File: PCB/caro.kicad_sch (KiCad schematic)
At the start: 9 parts, among them SW1 Power Switch, SW2 Control Button, U1 DFR0299

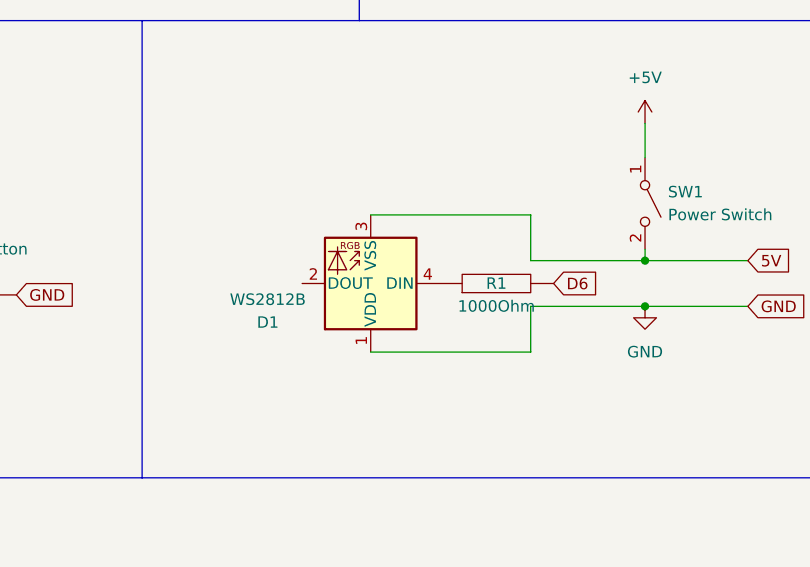
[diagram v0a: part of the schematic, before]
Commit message: Corrected inverted LED pins
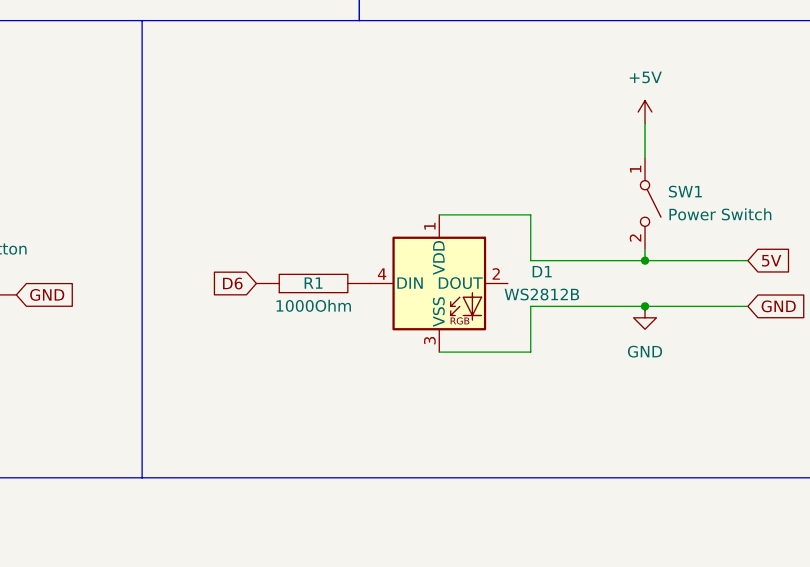
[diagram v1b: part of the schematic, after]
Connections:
- net 5V: now also D1.1 (VDD); no longer D1.3 (VSS)
- net D6: now also R1.1; no longer R1.2
- net GND: now also D1.3 (VSS); no longer D1.1 (VDD)
- net at D1.4 (DIN): now also R1.2; no longer R1.1
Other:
- moved on the sheet: D1, R1
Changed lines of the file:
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@@
     (stroke (width 0) (type default) (color 0 0 0 0))
   )
-  (wire (pts (xy 240.03 99.06) (xy 222.25 99.06))
-    (stroke (width 0) (type default) (color 0 0 0 0))
-  )
-  (wire (pts (xy 240.03 114.3) (xy 222.25 114.3))
+  (wire (pts (xy 240.03 99.06) (xy 229.87 99.06))
+    (stroke (width 0) (type default) (color 0 0 0 0))
+  )
+  (wire (pts (xy 240.03 114.3) (xy 229.87 114.3))
     (stroke (width 0) (type default) (color 0 0 0 0))
   )
@@
     )
   )
-  (global_label "D6" (shape input) (at 242.57 106.68 0) (fields_autoplaced)
-    (effects (font (size 1.27 1.27)) (justify left))
-    (property "Intersheet References" "${INTERSHEET_REFS}" (id 0) (at 247.4626 106.6006 0)
-      (effects (font (size 1.27 1.27)) (justify left) hide)
+  (global_label "D6" (shape input) (at 209.55 106.68 180) (fields_autoplaced)
+    (effects (font (size 1.27 1.27)) (justify right))
+    (property "Intersheet References" "${INTERSHEET_REFS}" (id 0) (at 204.6574 106.7594 0)
+      (effects (font (size 1.27 1.27)) (justify right) hide)
     )
   )
@@
     (pin "1")
   )
-  (symbol (lib_id "pspice:R") (at 236.22 106.68 90) (unit 1)
-    (in_bom yes) (on_board yes)
-    (property "Reference" "R1" (id 0) (at 236.22 106.68 90))
-    (property "Value" "1000Ohm" (id 1) (at 236.22 109.22 90))
-    (property "Footprint" "Resistor_THT:R_Axial_DIN0309_L9.0mm_D3.2mm_P20.32mm_Horizontal" (id 2) (at 236.22 106.68 0)
-      (effects (font (size 1.27 1.27)) hide)
-    )
-    (property "Datasheet" "~" (id 3) (at 236.22 106.68 0)
+  (symbol (lib_id "pspice:R") (at 215.9 106.68 90) (unit 1)
+    (in_bom yes) (on_board yes)
+    (property "Reference" "R1" (id 0) (at 215.9 106.68 90))
+    (property "Value" "1000Ohm" (id 1) (at 215.9 109.22 90))
+    (property "Footprint" "Resistor_THT:R_Axial_DIN0309_L9.0mm_D3.2mm_P20.32mm_Horizontal" (id 2) (at 215.9 106.68 0)
+      (effects (font (size 1.27 1.27)) hide)
+    )
+    (property "Datasheet" "~" (id 3) (at 215.9 106.68 0)
       (effects (font (size 1.27 1.27)) hide)
     )
@@
     (pin "9")
   )
-  (symbol (lib_id "LED:WS2812B") (at 222.25 106.68 180) (unit 1)
-    (in_bom yes) (on_board yes) (fields_autoplaced)
-    (property "Reference" "D1" (id 0) (at 210.82 111.0107 0))
-    (property "Value" "WS2812B" (id 1) (at 210.82 108.4707 0))
-    (property "Footprint" "Connector_PinHeader_2.54mm:PinHeader_1x03_P2.54mm_Vertical" (id 2) (at 220.98 99.06 0)
+  (symbol (lib_id "LED:WS2812B") (at 229.87 106.68 0) (unit 1)
+    (in_bom yes) (on_board yes)
+    (property "Reference" "D1" (id 0) (at 241.3 105.41 0))
+    (property "Value" "WS2812B" (id 1) (at 241.3 107.95 0))
+    (property "Footprint" "Connector_PinHeader_2.54mm:PinHeader_1x03_P2.54mm_Vertical" (id 2) (at 231.14 114.3 0)
       (effects (font (size 1.27 1.27)) (justify left top) hide)
     )
-    (property "Datasheet" "https://cdn-shop.adafruit.com/datasheets/WS2812B.pdf" (id 3) (at 219.71 97.155 0)
+    (property "Datasheet" "https://cdn-shop.adafruit.com/datasheets/WS2812B.pdf" (id 3) (at 232.41 116.205 0)
       (effects (font (size 1.27 1.27)) (justify left top) hide)
     )

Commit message: Bump to v1.1
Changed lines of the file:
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@@
+    (stroke (width 0) (type default) (color 0 0 0 0))
+  )
+  (wire (pts (xy 207.01 106.68) (xy 209.55 106.68))
     (stroke (width 0) (type default) (color 0 0 0 0))
   )
@@
     )
   )
-  (global_label "D6" (shape input) (at 209.55 106.68 180) (fields_autoplaced)
+  (global_label "D6" (shape input) (at 207.01 106.68 180) (fields_autoplaced)
     (effects (font (size 1.27 1.27)) (justify right))
-    (property "Intersheet References" "${INTERSHEET_REFS}" (id 0) (at 204.6574 106.7594 0)
+    (property "Intersheet References" "${INTERSHEET_REFS}" (id 0) (at 202.1174 106.7594 0)
       (effects (font (size 1.27 1.27)) (justify right) hide)
     )

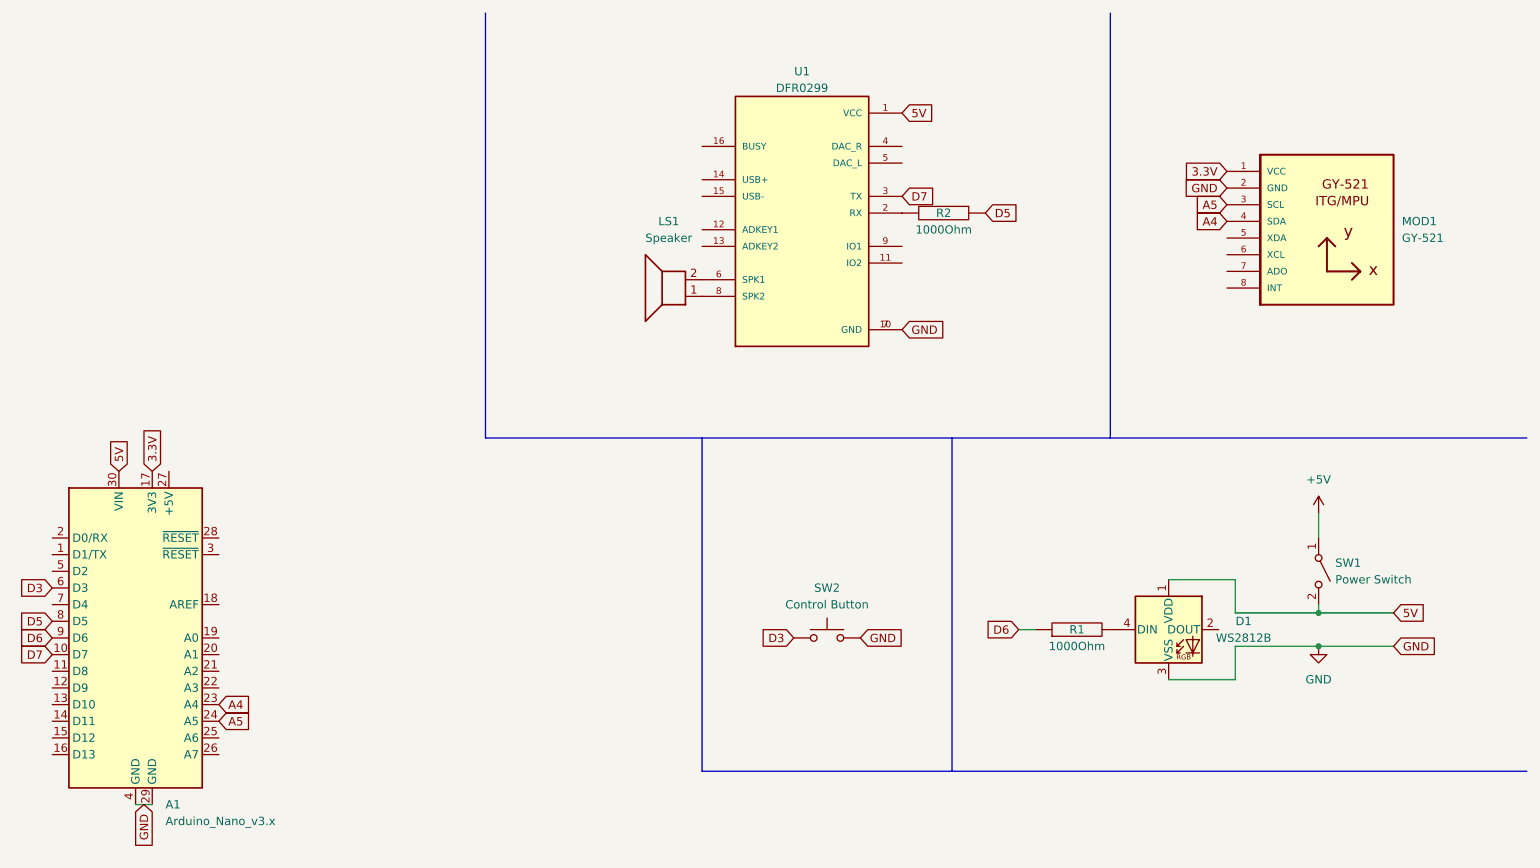
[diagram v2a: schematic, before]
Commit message: Updated annotations Added missing control LED Reduced resistor sizes
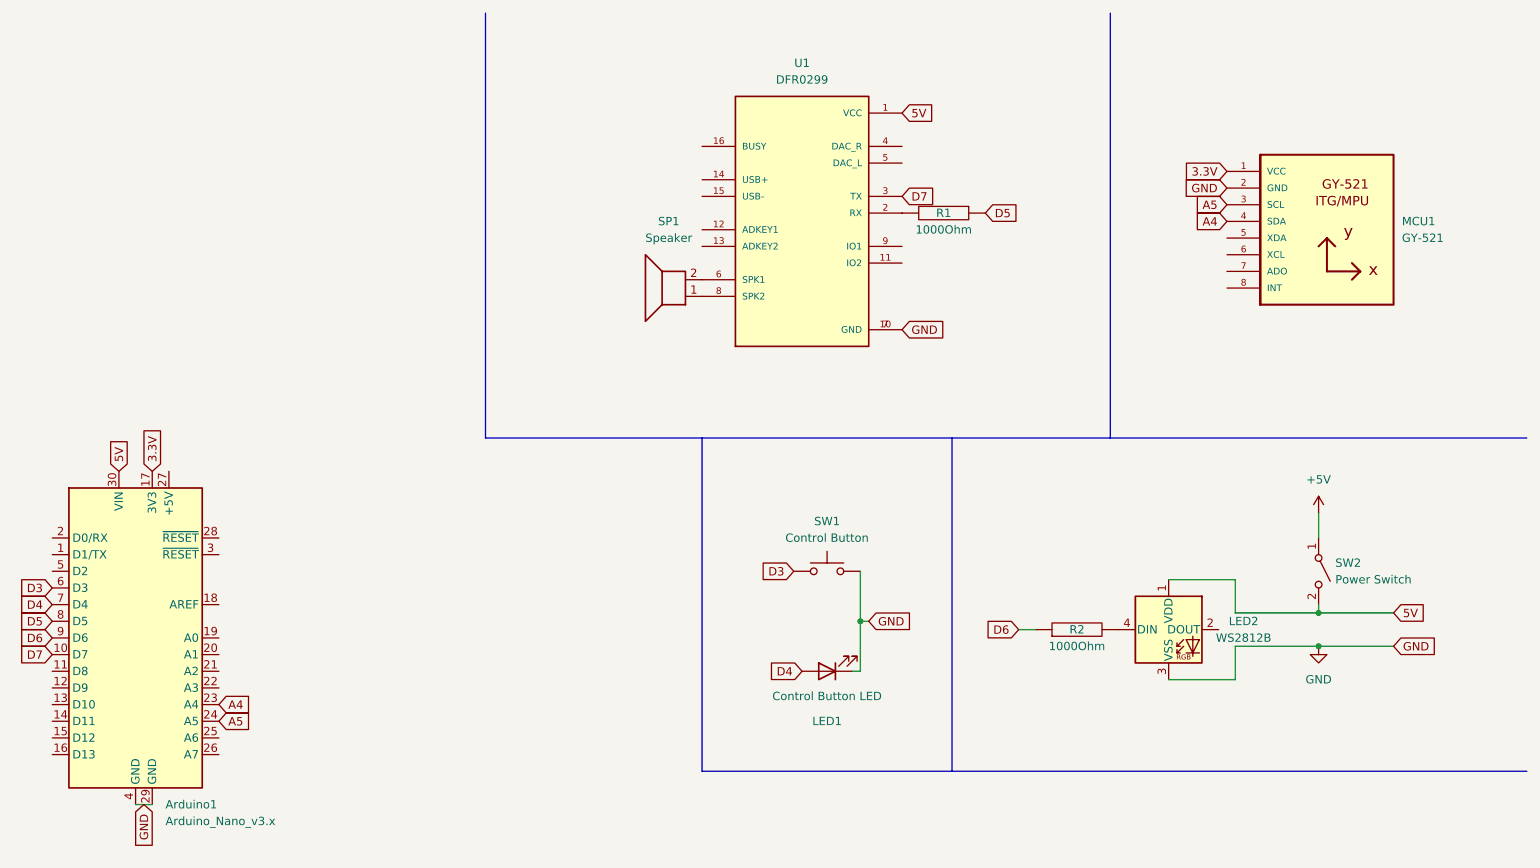
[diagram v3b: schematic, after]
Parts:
- added LED1: Control Button LED, Connector_PinHeader_2.54mm:PinHeader_2x01_P2.54mm_Vertical, symbol Device:LED
- R1: renamed from R2; footprint Resistor_THT:R_Axial_DIN0309_L9.0mm_D3.2mm_P20.32mm_Horizontal -> Resistor_THT:R_Axial_DIN0207_L6.3mm_D2.5mm_P10.16mm_Horizontal
- R2: renamed from R1; footprint Resistor_THT:R_Axial_DIN0309_L9.0mm_D3.2mm_P20.32mm_Horizontal -> Resistor_THT:R_Axial_DIN0207_L6.3mm_D2.5mm_P10.16mm_Horizontal
- renumbered A1 to Arduino1, D1 to LED2, MOD1 to MCU1, LS1 to SP1, SW2 to SW1, SW1 to SW2
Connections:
- net GND: now also LED1.1 (K)
- net D4: now reaches Arduino1.7 (D4)
- net D4: now also LED1.2 (A)
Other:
- moved on the sheet: SW1

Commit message: Revision v1.4 Swapped MCU and SDCard
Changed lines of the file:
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@@
     )
     (pin "1")
-    (pin "2")
     (pin "3")
     (pin "4")

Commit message: Corrected worng annotation
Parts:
- renumbered Arduino1 to U2
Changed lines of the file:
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@@
   (symbol (lib_id "MCU_Module:Arduino_Nano_v3.x") (at 72.39 107.95 0) (unit 1)
     (in_bom yes) (on_board yes) (fields_autoplaced)
-    (property "Reference" "Arduino1" (id 0) (at 76.9494 133.35 0)
+    (property "Reference" "U2" (id 0) (at 76.9494 133.35 0)
       (effects (font (size 1.27 1.27)) (justify left))
     )
@@
       (reference "#PWR02") (unit 1) (value "GND") (footprint "")
     )
-    (path "/ced11390-2682-4807-887b-321629abfbac"
-      (reference "Arduino1") (unit 1) (value "Arduino_Nano_v3.x") (footprint "Module:Arduino_Nano")
-    )
     (path "/ae1091f9-be9a-4c5e-a932-4d89f59d1190"
       (reference "LED1") (unit 1) (value "Control Button LED") (footprint "Connector_PinHeader_2.54mm:PinHeader_2x01_P2.54mm_Vertical")
@@
       (reference "U1") (unit 1) (value "DFR0299") (footprint "DFR0299:MODULE_DFR0299")
     )
+    (path "/ced11390-2682-4807-887b-321629abfbac"
+      (reference "U2") (unit 1) (value "Arduino_Nano_v3.x") (footprint "Module:Arduino_Nano")
+    )
   )

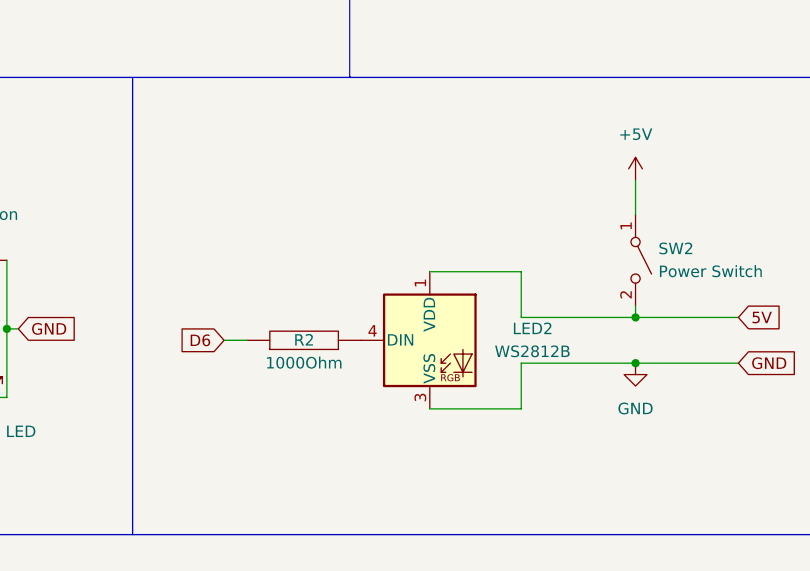
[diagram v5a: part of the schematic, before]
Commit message: Revision udate to v1.5 Swapped WS2812b to WS2811
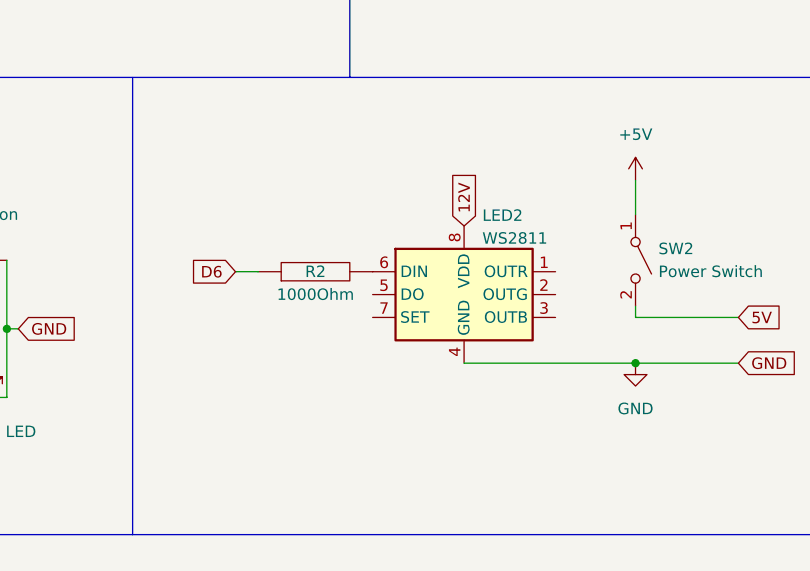
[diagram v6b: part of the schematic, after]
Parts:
- removed LED2: WS2812B, Connector_PinHeader_2.54mm:PinHeader_1x03_P2.54mm_Vertical, symbol LED:WS2812B
- added LED2: WS2811, Connector_PinHeader_2.54mm:PinHeader_1x02_P2.54mm_Vertical, symbol Driver_LED:WS2811
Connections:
- net GND: now also LED2.4 (GND)
- net at R2.2: now also LED2.6 (DIN)
- new net 12V: LED2.8 (VDD)
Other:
- moved on the sheet: R2
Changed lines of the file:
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@@
     (title "Carolyns Lightsaber")
   )
-  (junction (at 252.73 104.14) (diameter 0) (color 0 0 0 0)
-  )
   (junction (at 182.88 105.41) (diameter 0) (color 0 0 0 0)
   )
@@
     (stroke (width 0) (type default) (color 0 0 0 0))
   )
-  (wire (pts (xy 240.03 104.14) (xy 240.03 99.06))
-    (stroke (width 0) (type default) (color 0 0 0 0))
-  )
   (wire (pts (xy 182.88 97.79) (xy 182.88 105.41))
     (stroke (width 0) (type default) (color 0 0 0 0))
@@
     (stroke (width 0) (type default) (color 0 0 0 0))
   )
-  (wire (pts (xy 240.03 99.06) (xy 229.87 99.06))
-    (stroke (width 0) (type default) (color 0 0 0 0))
-  )
-  (wire (pts (xy 240.03 114.3) (xy 229.87 114.3))
-    (stroke (width 0) (type default) (color 0 0 0 0))
-  )
-  (wire (pts (xy 240.03 109.22) (xy 240.03 114.3))
-    (stroke (width 0) (type default) (color 0 0 0 0))
-  )
   (polyline (pts (xy 125.73 77.47) (xy 220.98 77.47))
     (stroke (width 0) (type default) (color 0 0 0 0))
@@
     (stroke (width 0) (type default) (color 0 0 0 0))
   )
-  (wire (pts (xy 207.01 106.68) (xy 209.55 106.68))
+  (wire (pts (xy 208.28 99.06) (xy 210.82 99.06))
     (stroke (width 0) (type default) (color 0 0 0 0))
   )
@@
     (stroke (width 0) (type default) (color 0 0 0 0))
   )
-  (wire (pts (xy 252.73 109.22) (xy 240.03 109.22))
-    (stroke (width 0) (type default) (color 0 0 0 0))
-  )
-  (wire (pts (xy 240.03 104.14) (xy 252.73 104.14))
+  (wire (pts (xy 233.68 109.22) (xy 252.73 109.22))
     (stroke (width 0) (type default) (color 0 0 0 0))
   )
@@
     )
   )
-  (global_label "D6" (shape input) (at 207.01 106.68 180) (fields_autoplaced)
-    (effects (font (size 1.27 1.27)) (justify right))
-    (property "Intersheet References" "${INTERSHEET_REFS}" (id 0) (at 202.1174 106.7594 0)
+  (global_label "D6" (shape input) (at 208.28 99.06 180) (fields_autoplaced)
+    (effects (font (size 1.27 1.27)) (justify right))
+    (property "Intersheet References" "${INTERSHEET_REFS}" (id 0) (at 203.3874 99.1394 0)
       (effects (font (size 1.27 1.27)) (justify right) hide)
     )
@@
     (effects (font (size 1.27 1.27)) (justify left))
     (property "Intersheet References" "${INTERSHEET_REFS}" (id 0) (at 270.4436 109.1406 0)
+      (effects (font (size 1.27 1.27)) (justify left) hide)
+    )
+  )
+  (global_label "12V" (shape input) (at 233.68 93.98 90) (fields_autoplaced)
+    (effects (font (size 1.27 1.27)) (justify left))
+    (property "Intersheet References" "${INTERSHEET_REFS}" (id 0) (at 233.6006 88.0593 90)
       (effects (font (size 1.27 1.27)) (justify left) hide)
     )
@@
     (pin "1")
   )
-  (symbol (lib_id "pspice:R") (at 215.9 106.68 90) (unit 1)
+  (symbol (lib_id "pspice:R") (at 217.17 99.06 90) (unit 1)
     (in_bom yes) (on_board yes)
-    (property "Reference" "R2" (id 0) (at 215.9 106.68 90))
-    (property "Value" "1000Ohm" (id 1) (at 215.9 109.22 90))
-    (property "Footprint" "Resistor_THT:R_Axial_DIN0207_L6.3mm_D2.5mm_P10.16mm_Horizontal" (id 2) (at 215.9 106.68 0)
-      (effects (font (size 1.27 1.27)) hide)
-    )
-    (property "Datasheet" "~" (id 3) (at 215.9 106.68 0)
+    (property "Reference" "R2" (id 0) (at 217.17 99.06 90))
+    (property "Value" "1000Ohm" (id 1) (at 217.17 101.6 90))
+    (property "Footprint" "Resistor_THT:R_Axial_DIN0207_L6.3mm_D2.5mm_P10.16mm_Horizontal" (id 2) (at 217.17 99.06 0)
+      (effects (font (size 1.27 1.27)) hide)
+    )
+    (property "Datasheet" "~" (id 3) (at 217.17 99.06 0)
       (effects (font (size 1.27 1.27)) hide)
     )
@@
     (pin "1")
     (pin "2")
+  )
+  (symbol (lib_id "Driver_LED:WS2811") (at 233.68 101.6 0) (unit 1)
+    (in_bom yes) (on_board yes) (fields_autoplaced)
+    (property "Reference" "LED2" (id 0) (at 235.6994 92.8202 0)
+      (effects (font (size 1.27 1.27)) (justify left))
+    )
+    (property "Value" "WS2811" (id 1) (at 235.6994 95.3571 0)
+      (effects (font (size 1.27 1.27)) (justify left))
+    )
+    (property "Footprint" "Connector_PinHeader_2.54mm:PinHeader_1x02_P2.54mm_Vertical" (id 2) (at 226.06 97.79 0)
+      (effects (font (size 1.27 1.27)) hide)
+    )
+    (property "Datasheet" "https://cdn-shop.adafruit.com/datasheets/WS2811.pdf" (id 3) (at 228.6 95.25 0)
+      (effects (font (size 1.27 1.27)) hide)
+    )
+    (pin "1")
+    (pin "2")
+    (pin "3")
+    (pin "4")
+    (pin "5")
+    (pin "6")
+    (pin "7")
+    (pin "8")
   )
   (symbol (lib_id "Device:LED") (at 177.8 113.03 180) (unit 1)
@@
     (pin "9")
   )
-  (symbol (lib_id "LED:WS2812B") (at 229.87 106.68 0) (unit 1)
-    (in_bom yes) (on_board yes)
-    (property "Reference" "LED2" (id 0) (at 241.3 105.41 0))
-    (property "Value" "WS2812B" (id 1) (at 241.3 107.95 0))
-    (property "Footprint" "Connector_PinHeader_2.54mm:PinHeader_1x03_P2.54mm_Vertical" (id 2) (at 231.14 114.3 0)
-      (effects (font (size 1.27 1.27)) (justify left top) hide)
-    )
-    (property "Datasheet" "https://cdn-shop.adafruit.com/datasheets/WS2812B.pdf" (id 3) (at 232.41 116.205 0)
-      (effects (font (size 1.27 1.27)) (justify left top) hide)
-    )
-    (pin "1")
-    (pin "3")
-    (pin "4")
-  )
   (sheet_instances
     (path "/" (page "1"))
@@
       (reference "LED1") (unit 1) (value "Control Button LED") (footprint "Connector_PinHeader_2.54mm:PinHeader_2x01_P2.54mm_Vertical")
     )
-    (path "/fae879a5-9fbf-429c-afbb-d0c2bd3ef143"
-      (reference "LED2") (unit 1) (value "WS2812B") (footprint "Connector_PinHeader_2.54mm:PinHeader_1x03_P2.54mm_Vertical")
+    (path "/ac2d76c8-1ed7-4fe2-aa51-42daa0e3bc9c"
+      (reference "LED2") (unit 1) (value "WS2811") (footprint "Connector_PinHeader_2.54mm:PinHeader_1x02_P2.54mm_Vertical")
     )
     (path "/29aa335b-758f-477a-af4b-8a1558985f41"
